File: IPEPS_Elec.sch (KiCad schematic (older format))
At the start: 41 parts

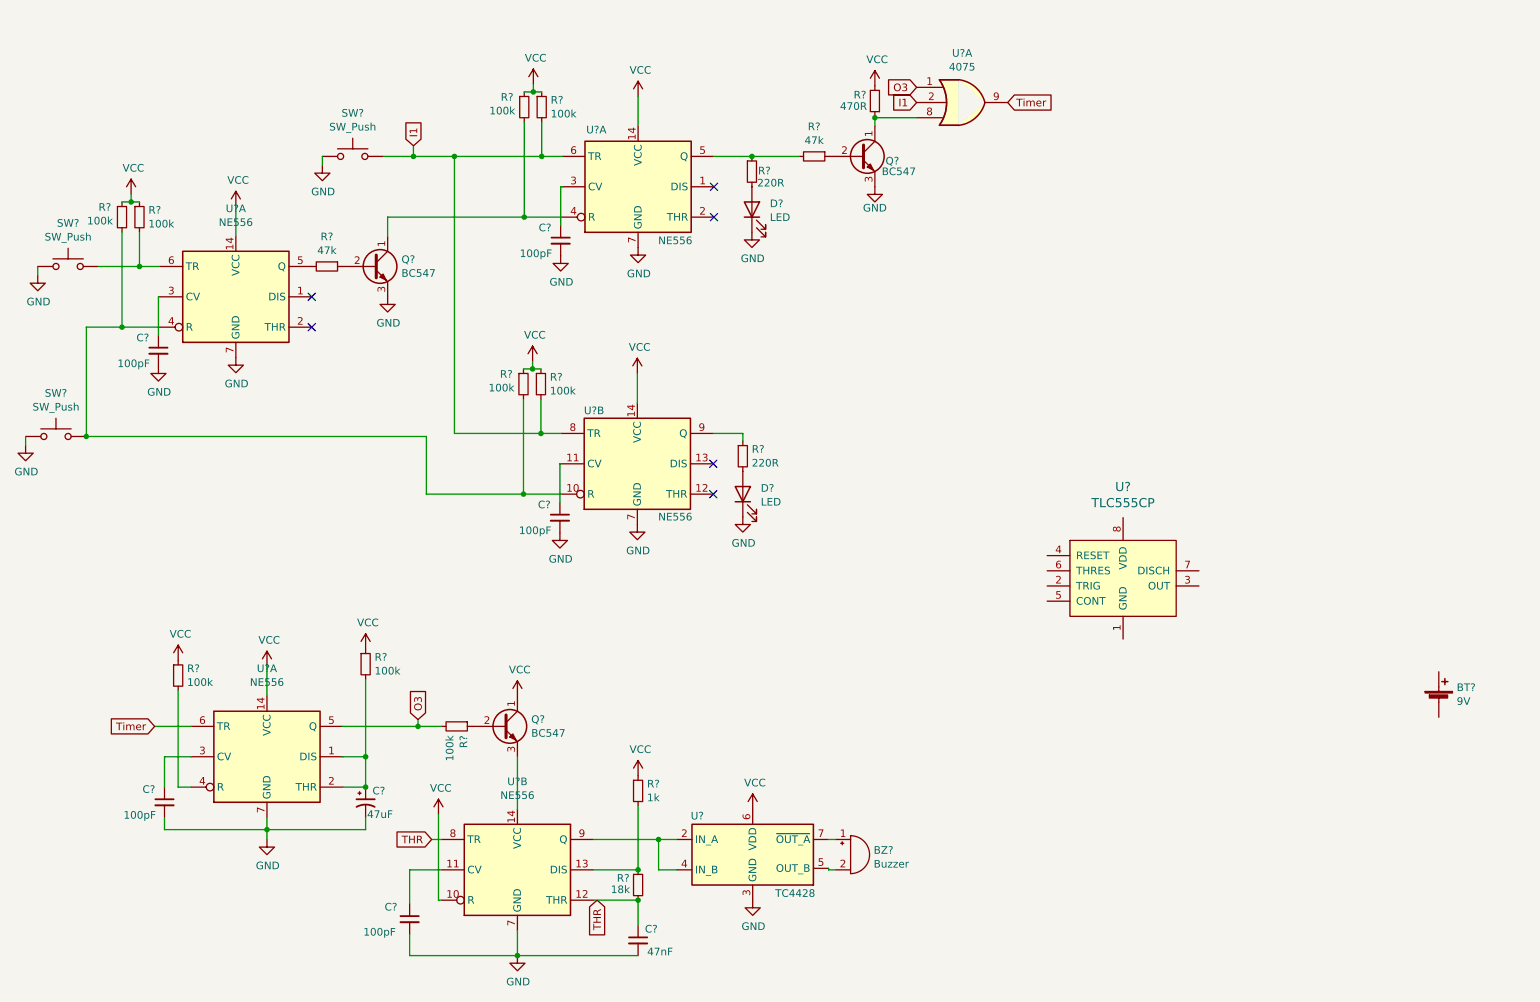
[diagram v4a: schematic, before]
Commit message: isolate the switches together
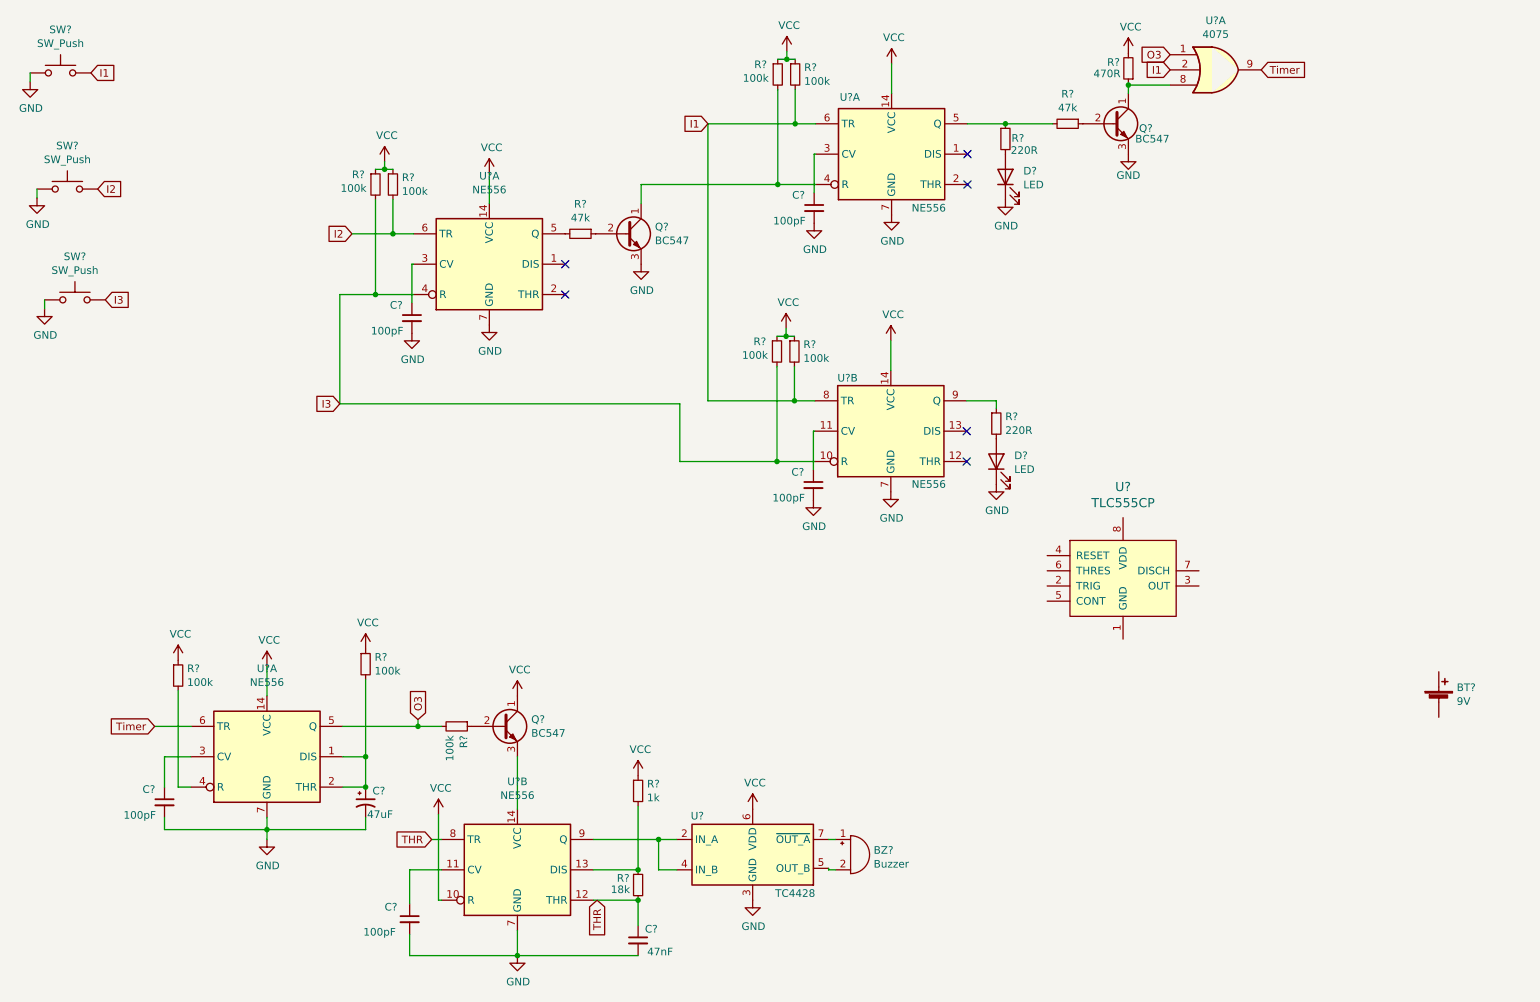
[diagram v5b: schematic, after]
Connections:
- net I3: now reaches R?.2, R?.2, SW?.2, U?.10 (R), U?.4 (R)
- net I2: now reaches R?.2, SW?.2, U?.6 (TR)
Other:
- moved on the sheet: C?, D?, Q?, R?, SW?, U?A, U?B

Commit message: reorganise and label components
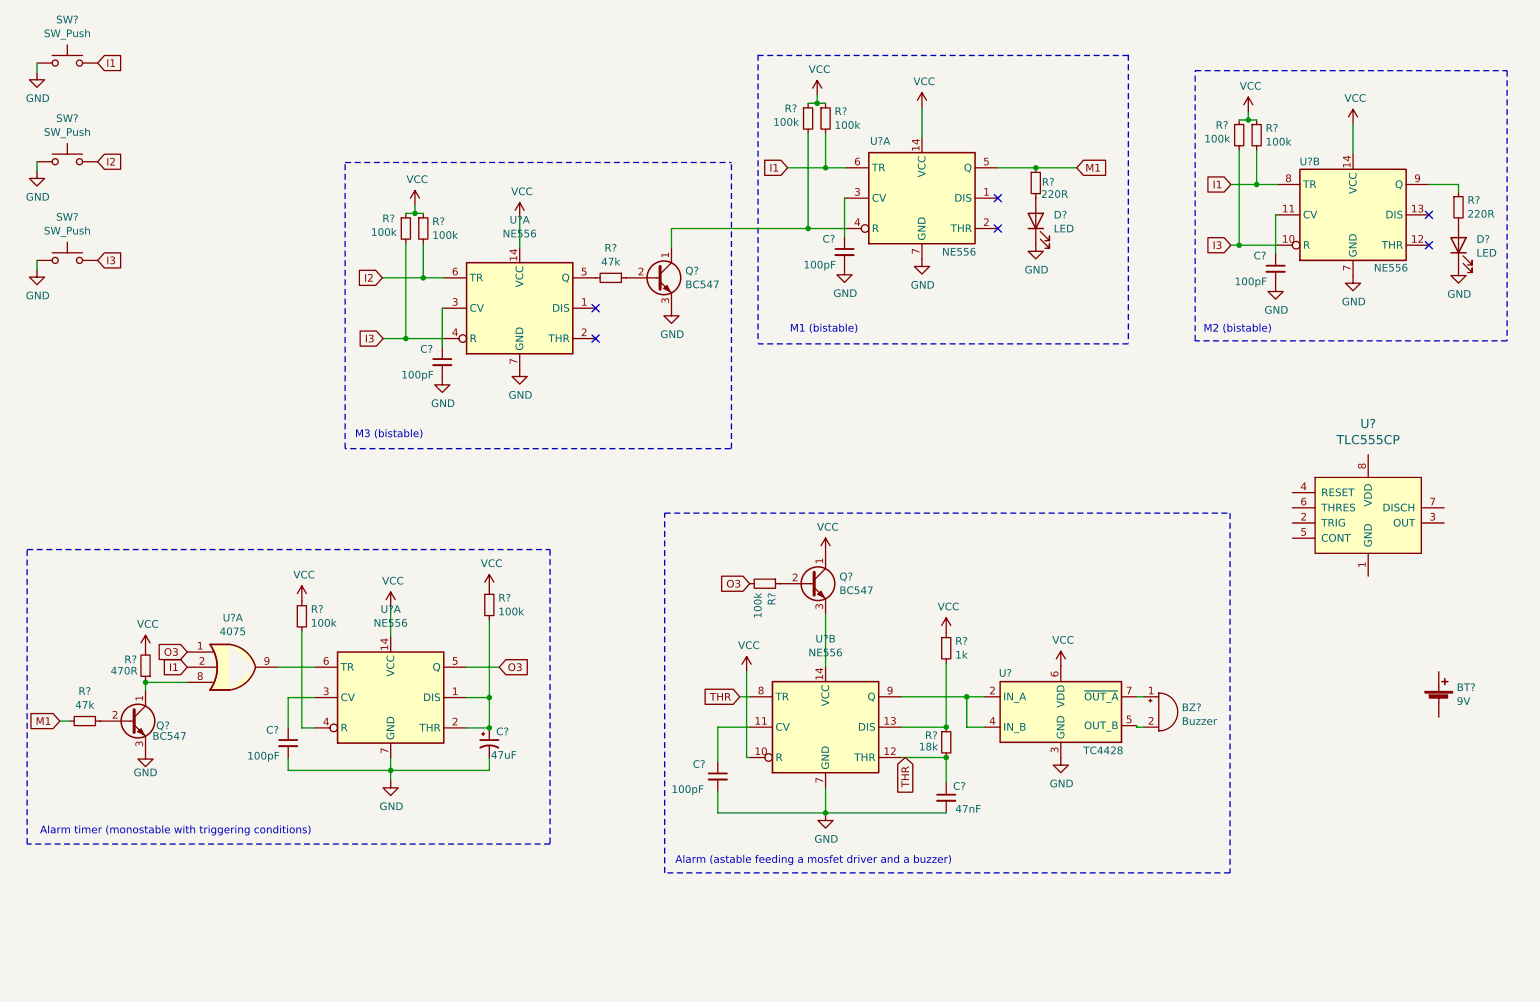
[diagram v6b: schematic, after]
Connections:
- net M1: now reaches R?.1, R?.2, U?.5 (Q)
- net Timer: no longer names the net of U?.6 (TR), U?.9
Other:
- note added: "Alarm (astable feeding a mosfet driver and a buzzer)"
- note added: "Alarm timer (monostable with triggering conditions)"
- note added: "M1 (bistable)"
- note added: "M2 (bistable)"
- note added: "M3 (bistable)"
- moved on the sheet: BZ?, C?, D?, Q?, R?, SW?, U?, U?A, U?B
